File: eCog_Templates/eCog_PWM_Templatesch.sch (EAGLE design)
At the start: 1 part

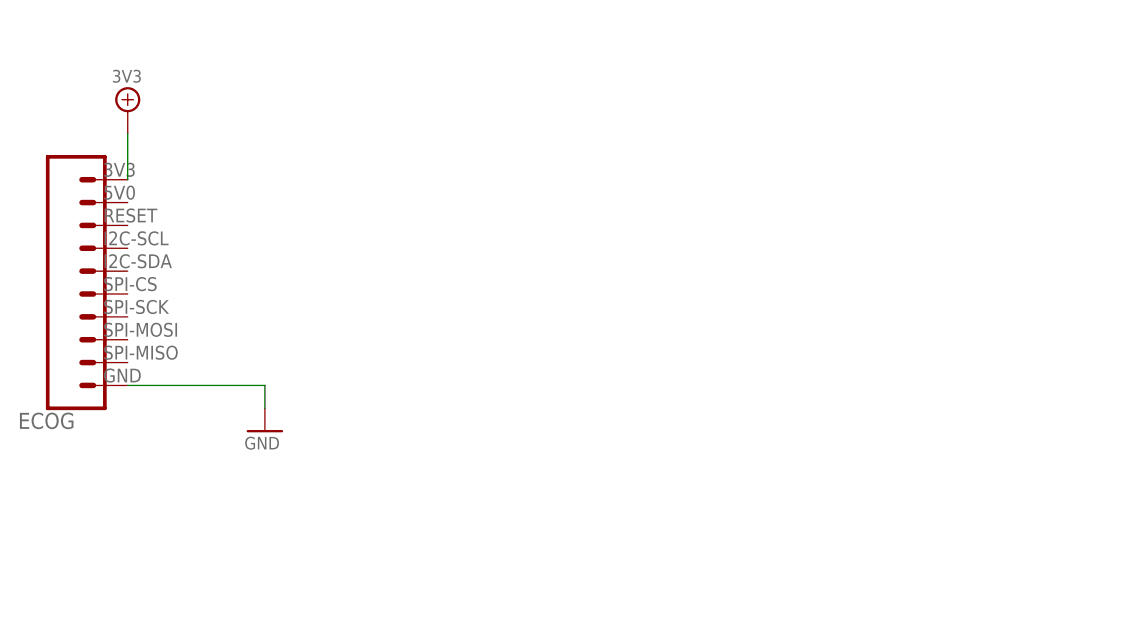
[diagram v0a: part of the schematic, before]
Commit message: Change to through hole and give bette descriptions.
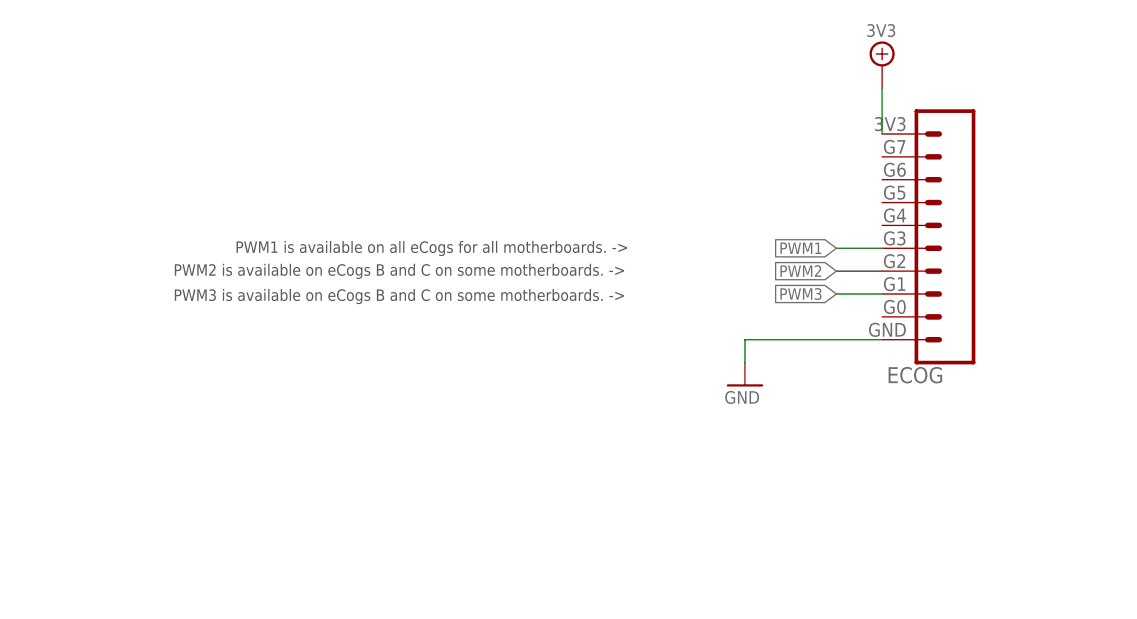
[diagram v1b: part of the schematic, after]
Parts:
- ECOG: value ECOG_BUSES_ROWTHROUGHHOLE -> ECOG_GENERAL_ROWTHROUGHOLE; device eCogs:ECOG_BUSES_ROWTHROUGHHOLE -> eCogs:ECOG_GENERAL_ROWTHROUGHOLE
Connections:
- new net PWM1: ECOG.G3
- new net PWM2: ECOG.G2
- new net PWM3: ECOG.G1
- net 3V3: now also ECOG.3V3; no longer ECOG.3V3@B8
- net GND: now also ECOG.GND; no longer ECOG.GND@B
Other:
- note added: "PWM1 is available on all eCogs for all motherboards. ->"
- note added: "PWM2 is available on eCogs B and C on some motherboards. ->"
- note added: "PWM3 is available on eCogs B and C on some motherboards. ->"
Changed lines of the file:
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@@
 <parts>
 <part name="FRAME1" library="frames" deviceset="A3L-LOC" device=""/>
-<part name="ECOG" library="eCogs" deviceset="ECOG_BUSES_ROW" device="THROUGHHOLE" value="ECOG_BUSES_ROWTHROUGHHOLE"/>
+<part name="ECOG" library="eCogs" deviceset="ECOG_GENERAL_ROW" device="THROUGHOLE" value="ECOG_GENERAL_ROWTHROUGHOLE"/>
+<part name="3V3_PWR1" library="eCogs" deviceset="3V3" device=""/>
 <part name="GND1" library="eCogs" deviceset="GND" device=""/>
-<part name="3V3_PWR1" library="eCogs" deviceset="3V3" device=""/>
 </parts>
 <sheets>
@@
 <text x="317.5" y="30.48" size="2.1844" layer="91">Copyright 2016 Gadget Factory, LLC</text>
 <text x="317.5" y="25.4" size="1.778" layer="91">See more details at www.GadgetFactory.net</text>
+<text x="75.438" y="70.612" size="1.27" layer="97">PWM1 is available on all eCogs for all motherboards. -&gt;</text>
+<text x="68.58" y="68.072" size="1.27" layer="97">PWM2 is available on eCogs B and C on some motherboards. -&gt;</text>
+<text x="68.58" y="65.278" size="1.27" layer="97">PWM3 is available on eCogs B and C on some motherboards. -&gt;</text>
 </plain>
 <instances>
 <instance part="FRAME1" gate="G$1" x="0" y="0"/>
-<instance part="ECOG" gate="ECOG_BUSES" x="55.88" y="53.34"/>
-<instance part="GND1" gate="A" x="78.74" y="50.8"/>
-<instance part="3V3_PWR1" gate="A" x="63.5" y="86.36"/>
+<instance part="ECOG" gate="ECOG_GENERAL" x="152.4" y="58.42"/>
+<instance part="3V3_PWR1" gate="A" x="147.32" y="91.44"/>
+<instance part="GND1" gate="A" x="132.08" y="55.88"/>
 </instances>
 <busses>
 </busses>
 <nets>
+<net name="3V3" class="0">
+<segment>
+<pinref part="ECOG" gate="ECOG_GENERAL" pin="3V3"/>
+<pinref part="3V3_PWR1" gate="A" pin="3V3"/>
+<wire x1="147.32" y1="83.82" x2="147.32" y2="88.9" width="0.2032" layer="91"/>
+</segment>
+</net>
 <net name="GND" class="0">
 <segment>
-<pinref part="ECOG" gate="ECOG_BUSES" pin="GND@B"/>
+<pinref part="ECOG" gate="ECOG_GENERAL" pin="GND"/>
 <pinref part="GND1" gate="A" pin="GND"/>
-<wire x1="63.5" y1="55.88" x2="78.74" y2="55.88" width="0.2032" layer="91"/>
-<wire x1="78.74" y1="55.88" x2="78.74" y2="53.34" width="0.2032" layer="91"/>
+<wire x1="147.32" y1="60.96" x2="132.08" y2="60.96" width="0.2032" layer="91"/>
+<wire x1="132.08" y1="60.96" x2="132.08" y2="58.42" width="0.2032" layer="91"/>
 </segment>
 </net>
-<net name="3V3" class="0">
+<net name="PWM1" class="0">
 <segment>
-<pinref part="3V3_PWR1" gate="A" pin="3V3"/>
-<pinref part="ECOG" gate="ECOG_BUSES" pin="3V3@B8"/>
-<wire x1="63.5" y1="83.82" x2="63.5" y2="78.74" width="0.2032" layer="91"/>
+<pinref part="ECOG" gate="ECOG_GENERAL" pin="G3"/>
+<wire x1="147.32" y1="71.12" x2="142.24" y2="71.12" width="0.2032" layer="91"/>
+<label x="142.24" y="71.12" size="1.27" layer="95" rot="R180" xref="yes"/>
 </segment>
 </net>
+<net name="PWM2" class="0">
+<segment>
+<pinref part="ECOG" gate="ECOG_GENERAL" pin="G2"/>
+<wire x1="147.32" y1="68.58" x2="142.24" y2="68.58" width="0.2032" layer="91"/>
+<label x="142.24" y="68.58" size="1.27" layer="95" rot="R180" xref="yes"/>
+</segment>
+</net>
+<net name="PWM3" class="0">
+<segment>
+<pinref part="ECOG" gate="ECOG_GENERAL" pin="G1"/>
+<wire x1="147.32" y1="66.04" x2="142.24" y2="66.04" width="0.2032" layer="91"/>
+<label x="142.24" y="66.04" size="1.27" layer="95" rot="R180" xref="yes"/>
+</segment>
+</net>
